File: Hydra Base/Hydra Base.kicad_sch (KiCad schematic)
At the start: 2 parts, among them J1 Conn_01x04, U1 Hydra_Core

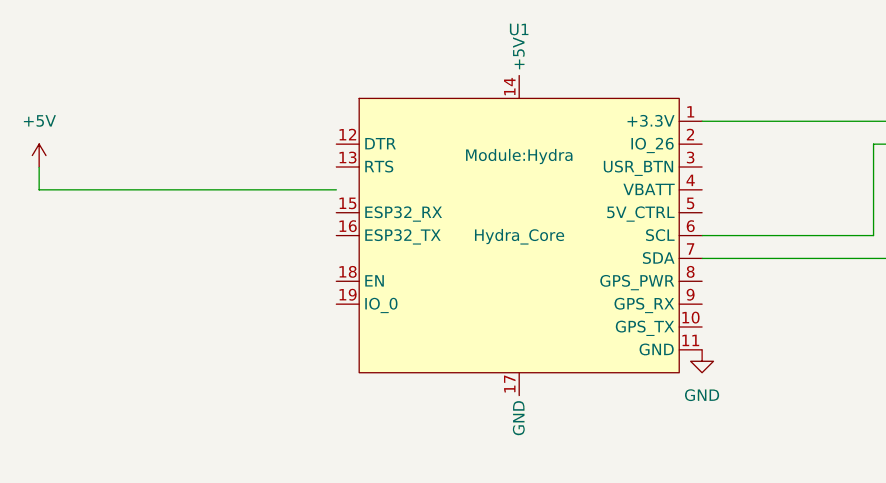
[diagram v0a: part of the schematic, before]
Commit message: footprint fixed
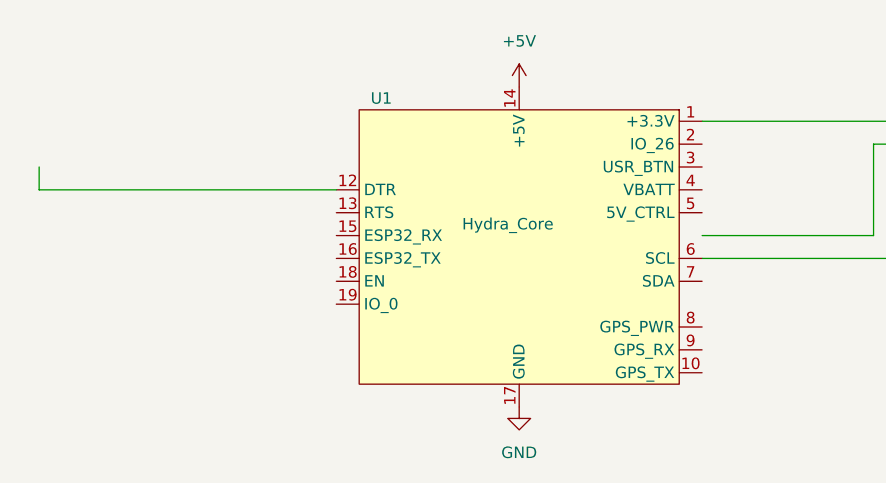
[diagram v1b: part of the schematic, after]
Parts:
- removed U1: Hydra_Core, Module:Hydra, symbol HydraLib:Hydra_Core
- added U1: Hydra_Core, core_pcb:Hydra_core, symbol hydra_core_symbol:Hydra_Core
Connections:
- net +5V: now also U1.14 (+5V)
- net GND: now also U1.11 (GND), U1.17 (GND)
- net at J1.1 (Pin_1): now also U1.1 (+3.3V)
- net at J1.3 (Pin_3): now also U1.6 (SCL)
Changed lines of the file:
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@@
     (stroke (width 0) (type default) (color 0 0 0 0))
   )
-  (symbol (lib_id "HydraLib:Hydra_Core") (at 134.62 68.58 0) (unit 1)
+  (symbol (lib_id "hydra_core_symbol:Hydra_Core") (at 134.62 68.58 0) (unit 1)
     (in_bom no) (on_board yes)
-    (property "Reference" "U1" (id 0) (at 134.62 44.45 0))
-    (property "Value" "Hydra_Core" (id 1) (at 134.62 67.31 0))
-    (property "Footprint" "Module:Hydra" (id 2) (at 134.62 58.42 0))
+    (property "Reference" "U1" (id 0) (at 118.11 52.07 0)
+      (effects (font (size 1.27 1.27)) (justify left))
+    )
+    (property "Value" "Hydra_Core" (id 1) (at 128.27 66.04 0)
+      (effects (font (size 1.27 1.27)) (justify left))
+    )
+    (property "Footprint" "core_pcb:Hydra_core" (id 2) (at 128.27 69.85 0)
+      (effects (font (size 1.27 1.27)) (justify left) hide)
+    )
     (property "Datasheet" "" (id 3) (at 134.62 64.77 0)
       (effects (font (size 1.27 1.27)) hide)
@@
     (pin "9")
   )
-  (symbol (lib_id "power:GND") (at 154.94 80.01 0) (unit 1)
+  (symbol (lib_id "power:GND") (at 134.62 86.36 0) (unit 1)
     (in_bom yes) (on_board yes) (fields_autoplaced)
-    (property "Reference" "#PWR01" (id 0) (at 154.94 86.36 0)
+    (property "Reference" "#PWR01" (id 0) (at 134.62 92.71 0)
       (effects (font (size 1.27 1.27)) hide)
     )
-    (property "Value" "GND" (id 1) (at 154.94 85.09 0))
-    (property "Footprint" "" (id 2) (at 154.94 80.01 0)
+    (property "Value" "GND" (id 1) (at 134.62 91.44 0))
+    (property "Footprint" "" (id 2) (at 134.62 86.36 0)
       (effects (font (size 1.27 1.27)) hide)
     )
-    (property "Datasheet" "" (id 3) (at 154.94 80.01 0)
+    (property "Datasheet" "" (id 3) (at 134.62 86.36 0)
       (effects (font (size 1.27 1.27)) hide)
     )
@@
     (pin "4")
   )
-  (symbol (lib_id "power:+5V") (at 81.28 59.69 0) (unit 1)
+  (symbol (lib_id "power:+5V") (at 134.62 50.8 0) (unit 1)
     (in_bom yes) (on_board yes) (fields_autoplaced)
-    (property "Reference" "#PWR0101" (id 0) (at 81.28 63.5 0)
+    (property "Reference" "#PWR0101" (id 0) (at 134.62 54.61 0)
       (effects (font (size 1.27 1.27)) hide)
     )
-    (property "Value" "+5V" (id 1) (at 81.28 54.61 0))
-    (property "Footprint" "" (id 2) (at 81.28 59.69 0)
+    (property "Value" "+5V" (id 1) (at 134.62 45.72 0))
+    (property "Footprint" "" (id 2) (at 134.62 50.8 0)
       (effects (font (size 1.27 1.27)) hide)
     )
-    (property "Datasheet" "" (id 3) (at 81.28 59.69 0)
+    (property "Datasheet" "" (id 3) (at 134.62 50.8 0)
       (effects (font (size 1.27 1.27)) hide)
     )
@@
       (reference "J1") (unit 1) (value "Conn_01x04") (footprint "Connector_PinHeader_2.54mm:PinHeader_1x04_P2.54mm_Vertical")
     )
-    (path "/0d8a9a27-34aa-4c7f-8587-c92687a91325"
-      (reference "U1") (unit 1) (value "Hydra_Core") (footprint "Module:Hydra")
+    (path "/253c3e2a-20f1-420f-b064-a89433b52227"
+      (reference "U1") (unit 1) (value "Hydra_Core") (footprint "core_pcb:Hydra_core")
     )
   )

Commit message: Primitive base board example
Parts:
- added BT1: Battery, Battery:BatteryHolder_MPD_BH-18650-PC2, symbol Device:Battery
- added J2: Screw_Terminal_01x02, TerminalBlock:TerminalBlock_Altech_AK300-2_P5.00mm, symbol Connector:Screw_Terminal_01x02
- added J3: Conn_01x02, Connector_PinHeader_2.54mm:PinHeader_1x02_P2.54mm_Vertical, symbol Connector_Generic:Conn_01x02
- added J4: Conn_01x02, Connector_JST:JST_PH_B2B-PH-K_1x02_P2.00mm_Vertical, symbol Connector_Generic:Conn_01x02
- added J5: Conn_01x04, Connector_PinHeader_2.54mm:PinHeader_1x04_P2.54mm_Vertical, symbol Connector_Generic:Conn_01x04
- added R1, R2: R, Resistor_THT:R_Axial_DIN0204_L3.6mm_D1.6mm_P5.08mm_Horizontal, symbol Device:R
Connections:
- net +5V: now also J2.1 (Pin_1)
- net GND: now also J1.2 (Pin_2), BT1.2 (-), J2.2 (Pin_2), J3.2 (Pin_2), J4.2 (Pin_2), J5.2 (Pin_2), R2.2; no longer J1.4 (Pin_4)
- net at U1.10 (GPS_TX): now also J5.4 (Pin_4)
- net at U1.3 (USR_BTN): now also J3.1 (Pin_1)
- net at U1.4 (VBATT): now also R1.2, R2.1
- net at U1.7 (SDA): now also J1.4 (Pin_4)
- net at U1.8 (GPS_PWR): now also J5.1 (Pin_1)
- net at U1.9 (GPS_RX): now also J5.3 (Pin_3)
- new net: BT1.1 (+), J4.1 (Pin_1), R1.1
